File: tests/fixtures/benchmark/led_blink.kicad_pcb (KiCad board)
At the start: 2 copper layers, 40 x 30 mm, 7 parts, among them J1 Power, SW1 ON/OFF

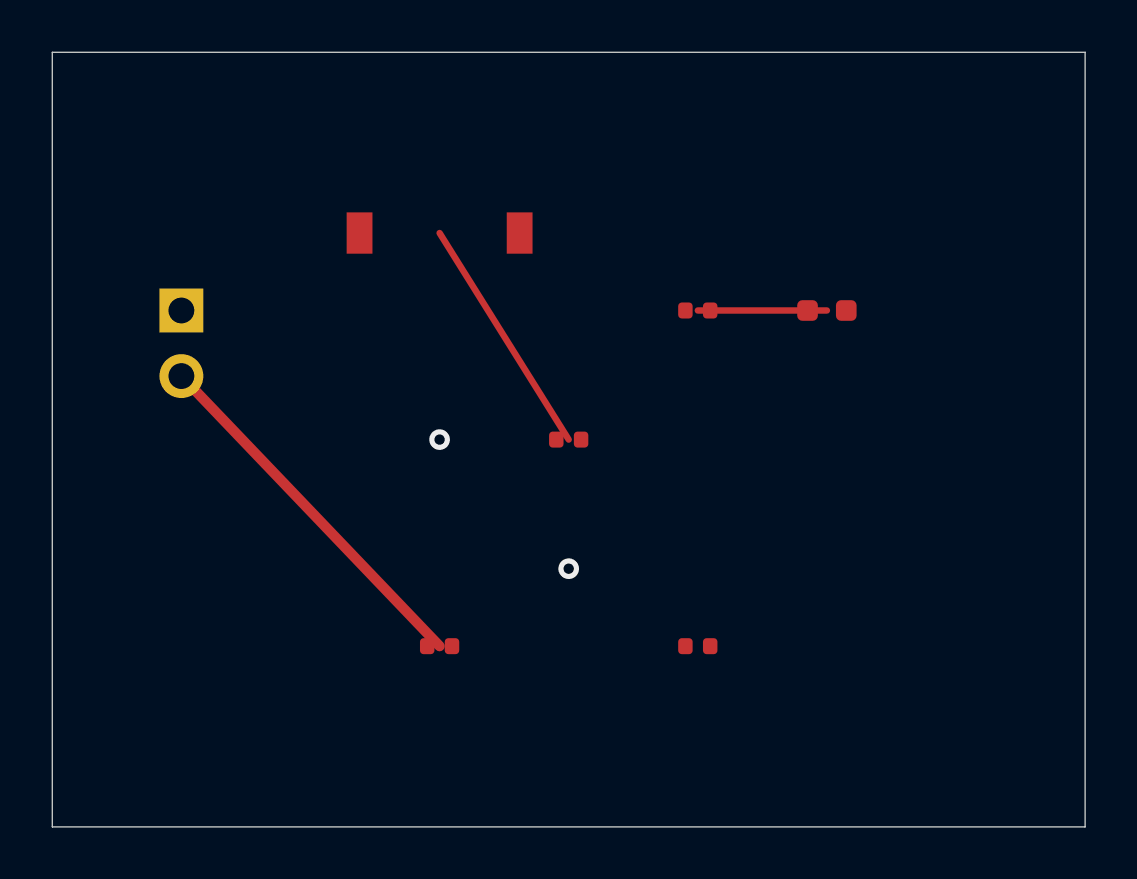
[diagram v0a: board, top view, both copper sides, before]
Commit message: fix(benchmark): the copper the fixtures shipped was lines between part centres
multi_ic reported 32 pieces of copper touching copper at 0.00mm before
anything was routed. Reading the segments settled what they were:

  (segment (start 65 45) (end 90 62) ...)
  (segment (start 90 62) (end 100 70) ...)
  (segment (start 100 70) (end 110 62) ...)

65,45 is U4's origin, 90,62 is C1's, 100,70 is U1's. These are straight lines
drawn between part centres, so they cross every package on the way and short
against the pads they pass. All three fixtures that carried copper carried the
same decoration, shorting 1, 13 and 32 times respectively.

Removed: 3 segments and 2 vias from led_blink, 8 and 4 from stm32_breakout, 15
and 10 from multi_ic. All three now ship zero shorts.

led_blink keeps copper and it is real copper: one trace from R1 pad 2 at
(120.48, 65) to D1 pad 1 at (124.25, 65), both on LED_ANODE, adjacent parts,
nothing in between. The import path still has a fixture to prove itself on
rather than losing the coverage along with the decoration.

Every ratchet is unchanged, which is the proof this fed no measurement:

  led_blink: 21 routes, 2 violations against 2, 0 shorts against 0
  stm32_breakout: 908 routes, 239 against 239, 136 shorts against 136
  multi_ic: 945 routes, 291 against 354, 187 shorts against 210
  shift_driver: 700 routes, 81 against 93, 33 shorts against 40
  qfp_fanout: 1478 routes, 309 against 376, 147 shorts against 260
  plane_board: 181 routes, 28 against 37, 13 shorts against 18

The benchmark routes from scratch and never read it. What did read it was
cypcb check, the viewer, and the CLI's board loader - everything a person
actually points at a board.

Three test files leaned on it and were repointed rather than deleted. The
parse expectations say 1 segment and 0 vias for led_blink and no copper for
the other two, and the origin test - which exists to catch copper imported
without subtracting the board corner - measures against the new trace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
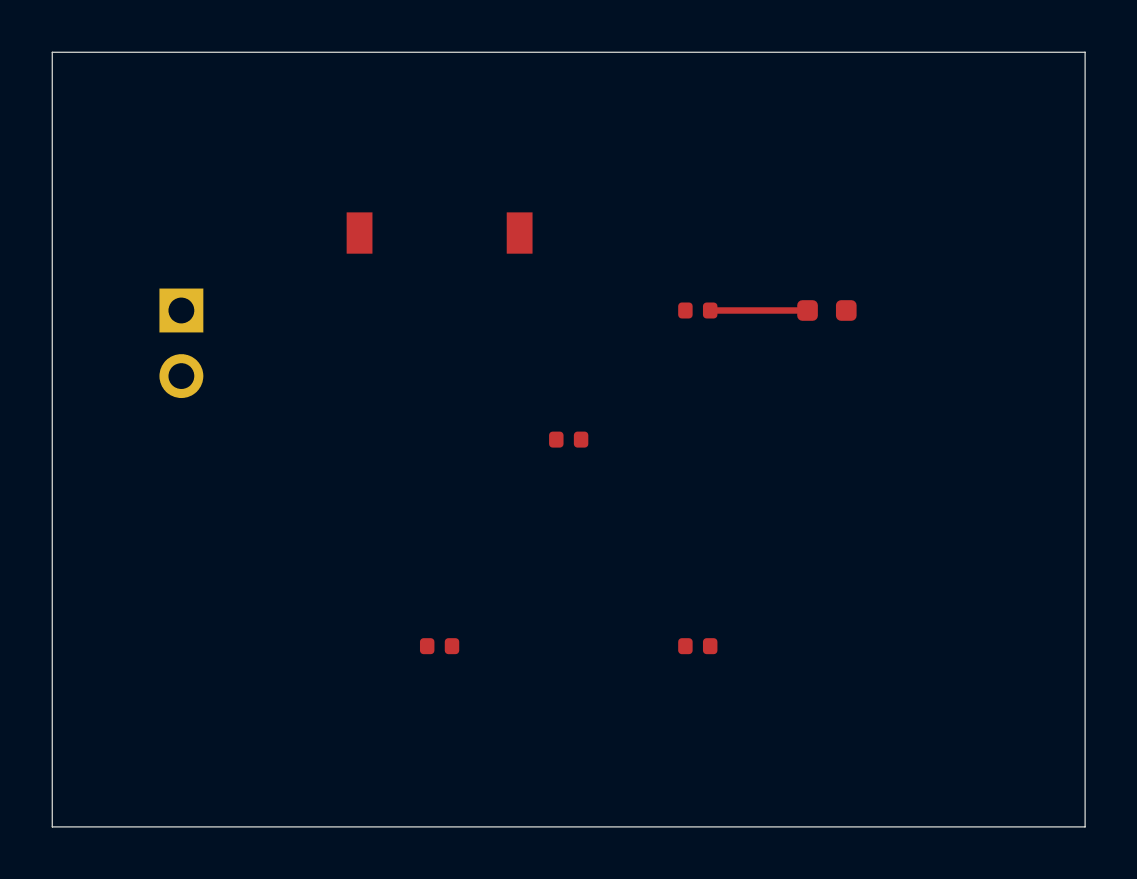
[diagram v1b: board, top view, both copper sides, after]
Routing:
- net GND: track 14.5 -> 0.00 mm, vias 1 -> 0
- net VCC: track 9.43 -> 0.00 mm, vias 1 -> 0
- net LED_ANODE: track 5.00 -> 3.77 mm
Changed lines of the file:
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@@
     )
   )
-  (segment (start 110 62) (end 115 70) (width 0.25) (layer "F.Cu") (net 1))
-  (segment (start 120 65) (end 125 65) (width 0.25) (layer "F.Cu") (net 3))
-  (segment (start 100 67.54) (end 110 78) (width 0.4) (layer "F.Cu") (net 2))
-  (via (at 115 75) (size 0.8) (drill 0.4) (layers "F.Cu" "B.Cu") (net 2))
-  (via (at 110 70) (size 0.8) (drill 0.4) (layers "F.Cu" "B.Cu") (net 1))
+  ; One real trace: R1 pad 2 to D1 pad 1, both on LED_ANODE.
+  (segment (start 120.48 65) (end 124.25 65) (width 0.25) (layer "F.Cu") (net 3))
 )
